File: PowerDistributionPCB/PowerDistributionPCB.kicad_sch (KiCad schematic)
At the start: 23 parts, among them J1 USB3_A, U1 Pico

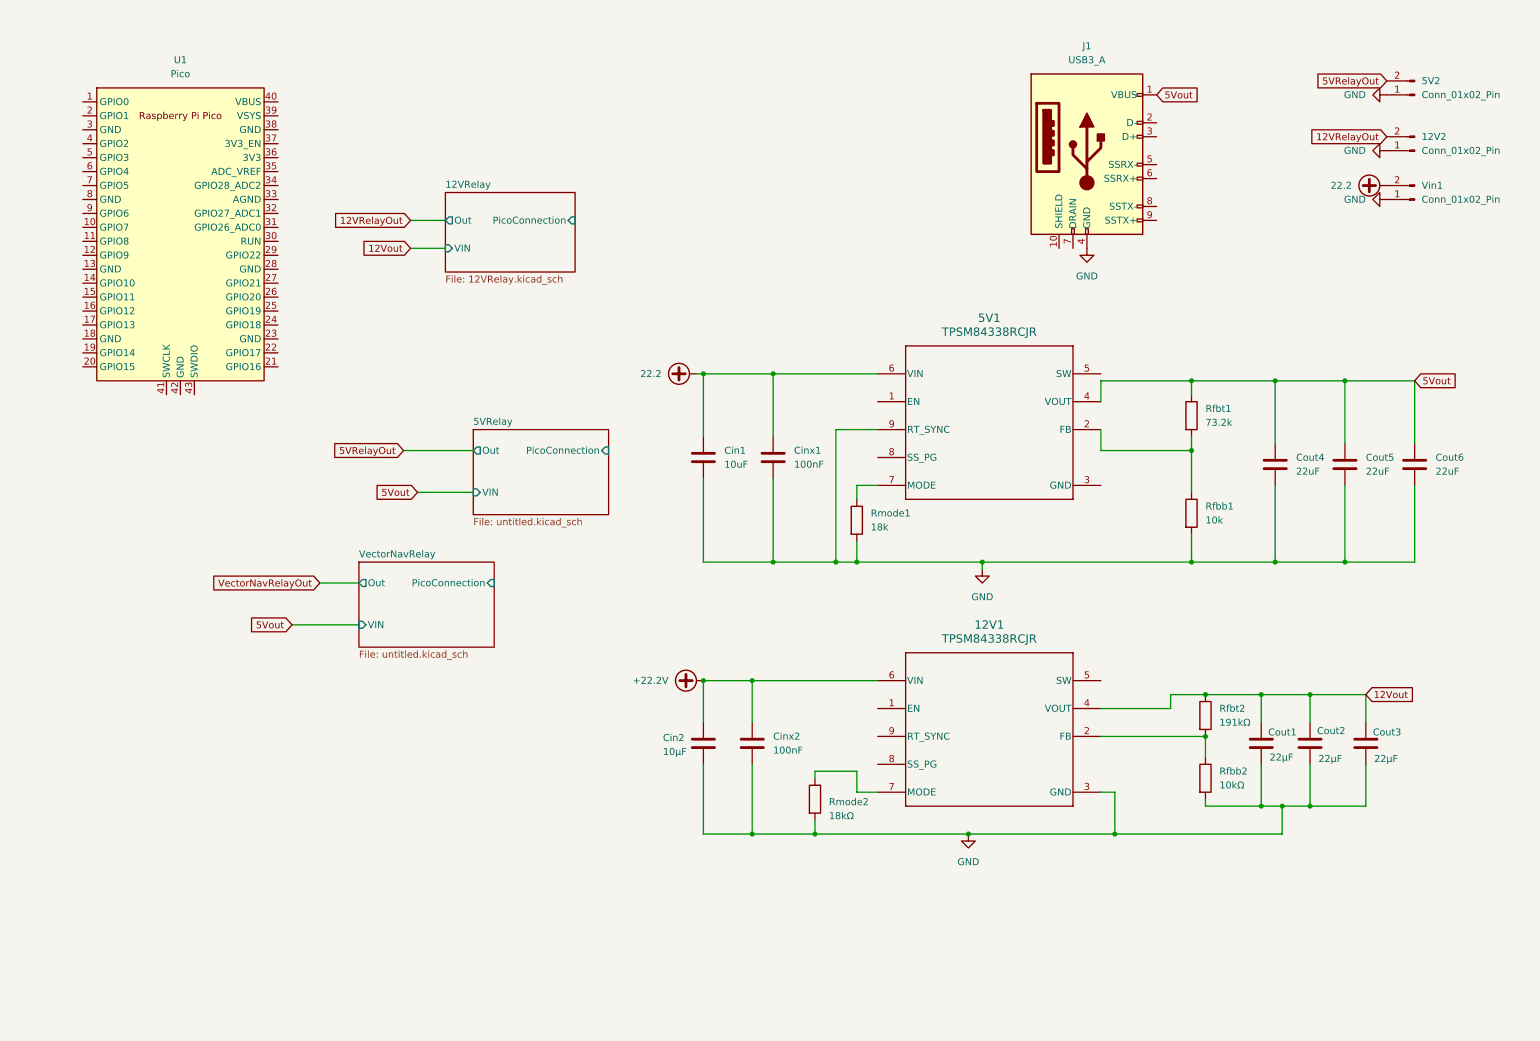
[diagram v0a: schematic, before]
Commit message: created sheet and updated USB connector
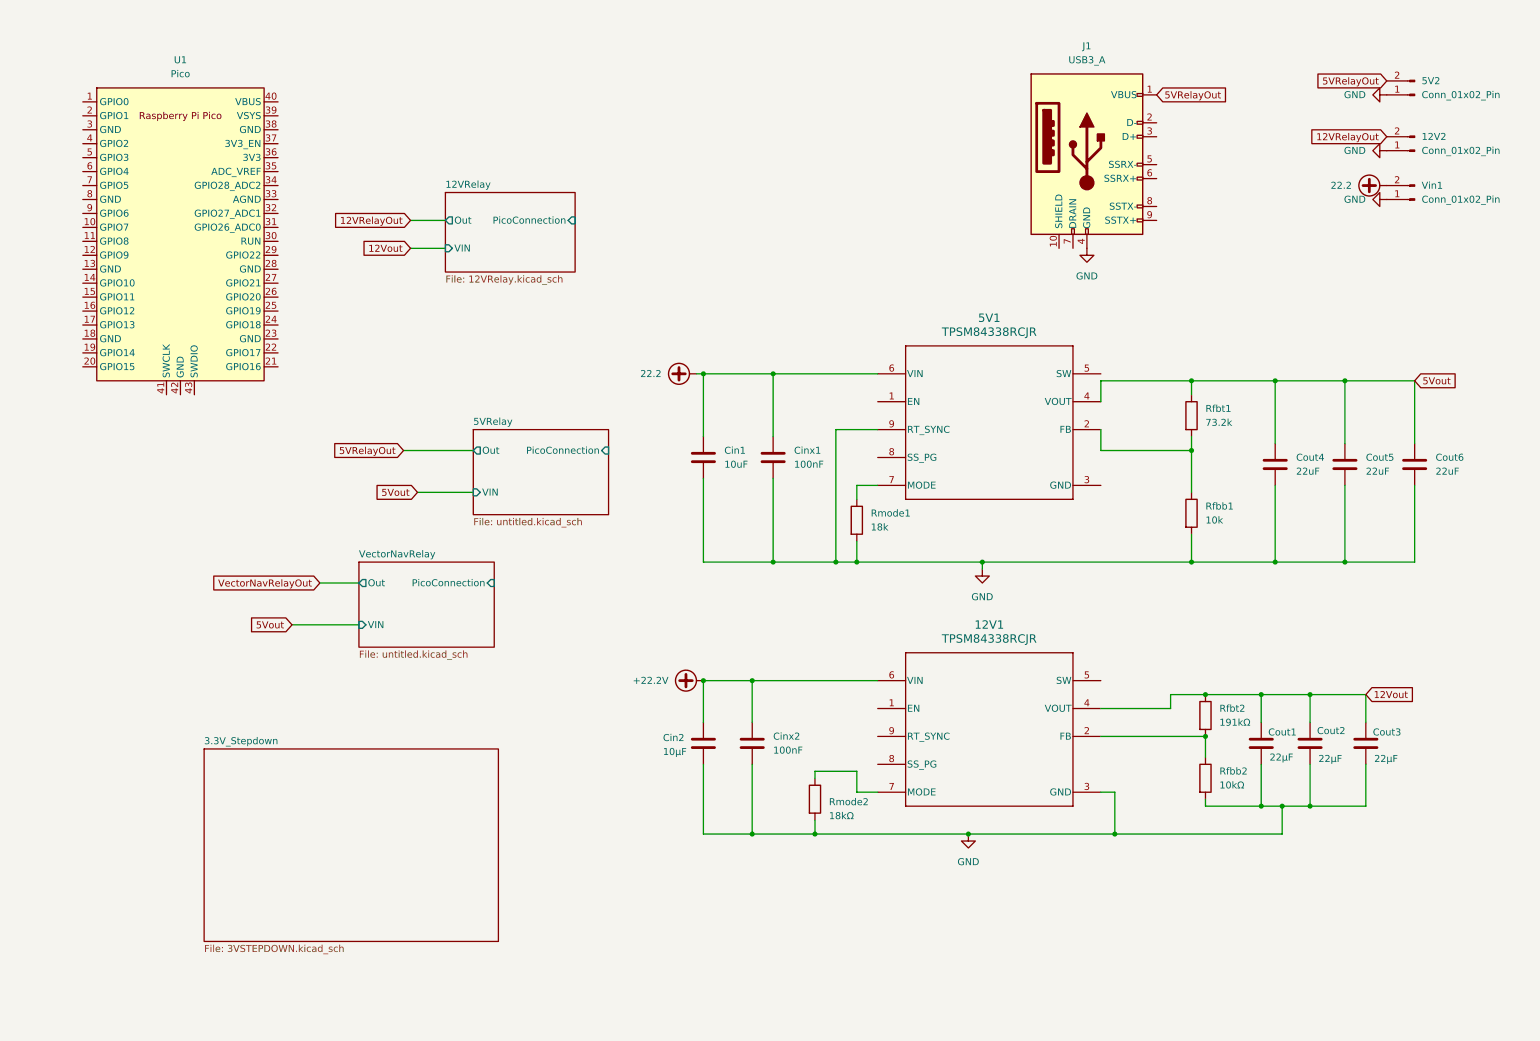
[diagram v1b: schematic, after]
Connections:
- net 5VRelayOut: now also J1.1 (VBUS)
- net 5Vout: no longer J1.1 (VBUS)
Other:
- added sheet 3.3V_Stepdown (3VSTEPDOWN.kicad_sch)
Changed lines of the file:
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@@
 		)
 	)
-	(global_label "5Vout"
+	(global_label "5VRelayOut"
 		(shape input)
-		(at 218.44 22.86 0)
+		(at 81.28 87.63 180)
 		(fields_autoplaced yes)
 		(effects
@@
 				(size 1.27 1.27)
 			)
-			(justify left)
+			(justify right)
 		)
 		(property "Intersheetrefs" "${INTERSHEET_REFS}"
-			(at 226.747 22.86 0)
-			(effects
-				(font
-					(size 1.27 1.27)
-				)
-				(justify left)
+			(at 67.6511 87.63 0)
+			(effects
+				(font
+					(size 1.27 1.27)
+				)
+				(justify right)
 				(hide yes)
 			)
@@
 	(global_label "5VRelayOut"
 		(shape input)
-		(at 81.28 87.63 180)
+		(at 218.44 22.86 0)
 		(fields_autoplaced yes)
 		(effects
@@
 				(size 1.27 1.27)
 			)
-			(justify right)
+			(justify left)
 		)
 		(property "Intersheetrefs" "${INTERSHEET_REFS}"
-			(at 67.6511 87.63 0)
-			(effects
-				(font
-					(size 1.27 1.27)
-				)
-				(justify right)
+			(at 232.0689 22.86 0)
+			(effects
+				(font
+					(size 1.27 1.27)
+				)
+				(justify left)
 				(hide yes)
 			)
@@
 				)
 			)
+		)
+	)
+	(sheet
+		(at 44.958 141.986)
+		(size 53.594 35.052)
+		(exclude_from_sim no)
+		(in_bom yes)
+		(on_board yes)
+		(dnp no)
+		(fields_autoplaced yes)
+		(stroke
+			(width 0.1524)
+			(type solid)
+		)
+		(fill
+			(color 0 0 0 0.0000)
+		)
+		(property "Sheetname" "3.3V_Stepdown"
+			(at 44.958 141.2744 0)
+			(effects
+				(font
+					(size 1.27 1.27)
+				)
+				(justify left bottom)
+			)
+		)
+		(property "Sheetfile" "3VSTEPDOWN.kicad_sch"
+			(at 44.958 177.6226 0)
+			(effects
+				(font
+					(size 1.27 1.27)
+				)
+				(justify left top)
+			)
+		)
+		(instances
+			(project "PowerDistributionPCB"
+				(path "/b27c75df-6223-4cc6-be69-062c2b02d5c6"
+					(page "5")
+				)
+			)

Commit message: switched pico to arduino, started implementing 3.3 relay and updated connections
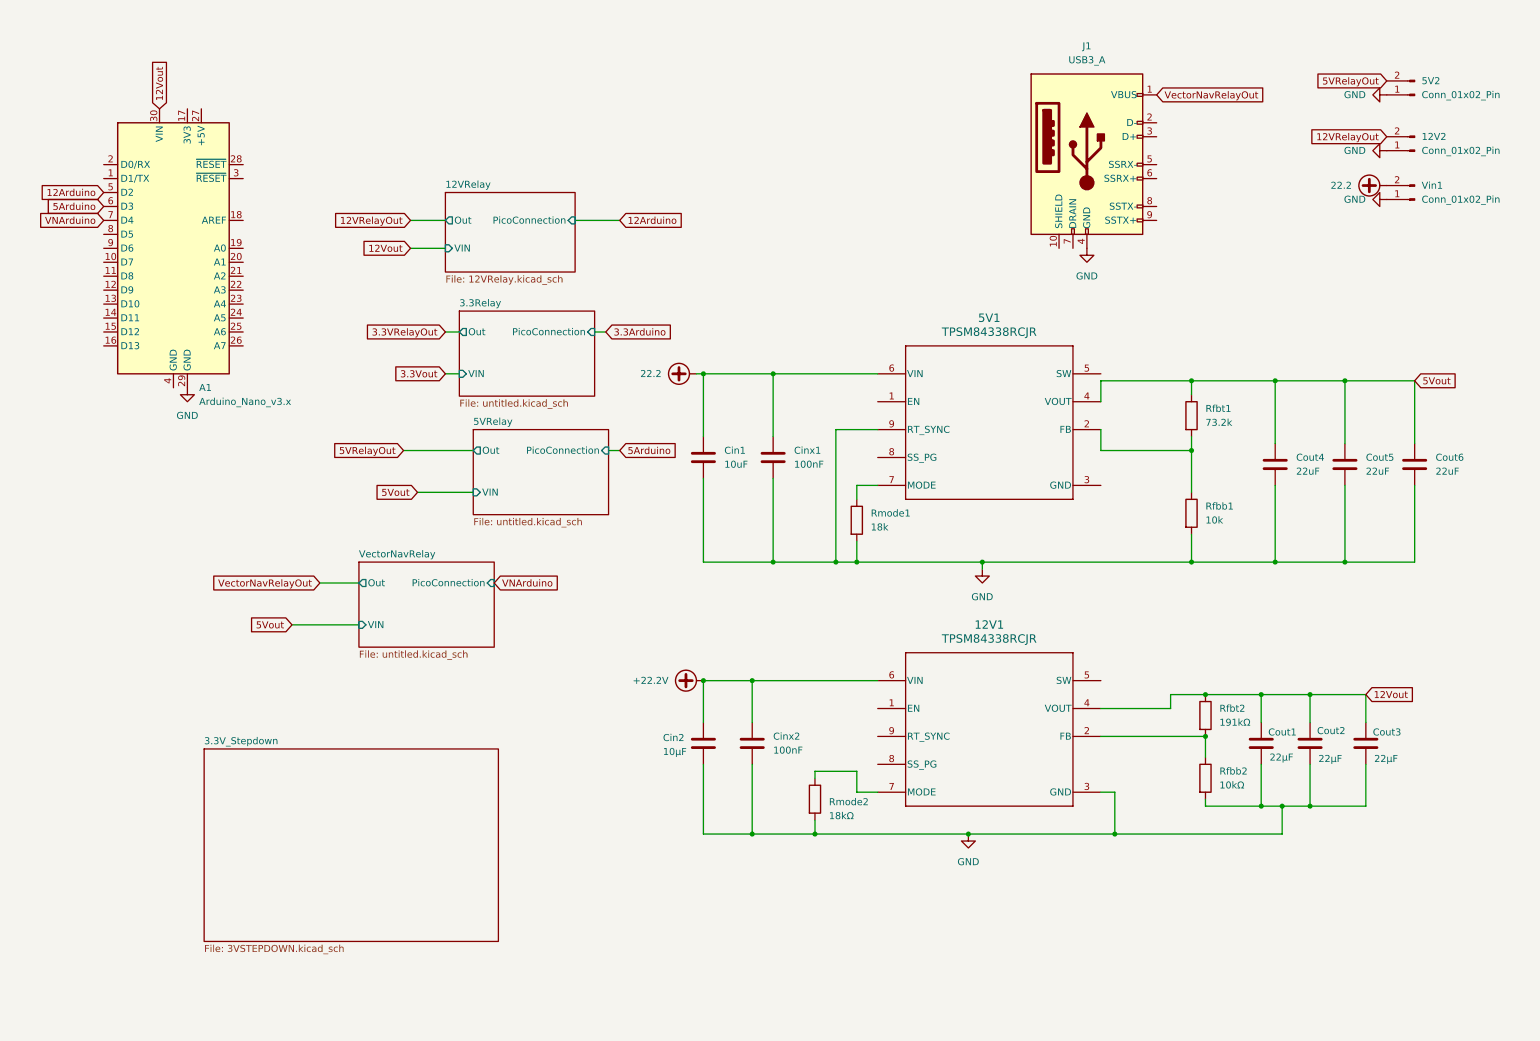
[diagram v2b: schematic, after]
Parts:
- removed U1: Pico, RPi_Pico:RPi_Pico_SMD_TH, symbol CustomComponents:Pico
- added A1: Arduino_Nano_v3.x, Module:Arduino_Nano, symbol MCU_Module:Arduino_Nano_v3.x
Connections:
- net 12Vout: now also A1.30 (VIN)
- net 5VRelayOut: no longer J1.1 (VBUS)
- net GND: now also A1.29 (GND)
- net VectorNavRelayOut: now also J1.1 (VBUS)
- new net 12Arduino: A1.5 (D2)
- new net 5Arduino: A1.6 (D3)
- new net VNArduino: A1.7 (D4)
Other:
- added sheet 3.3Relay (untitled.kicad_sch)

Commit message: started reworking relays for new relay design
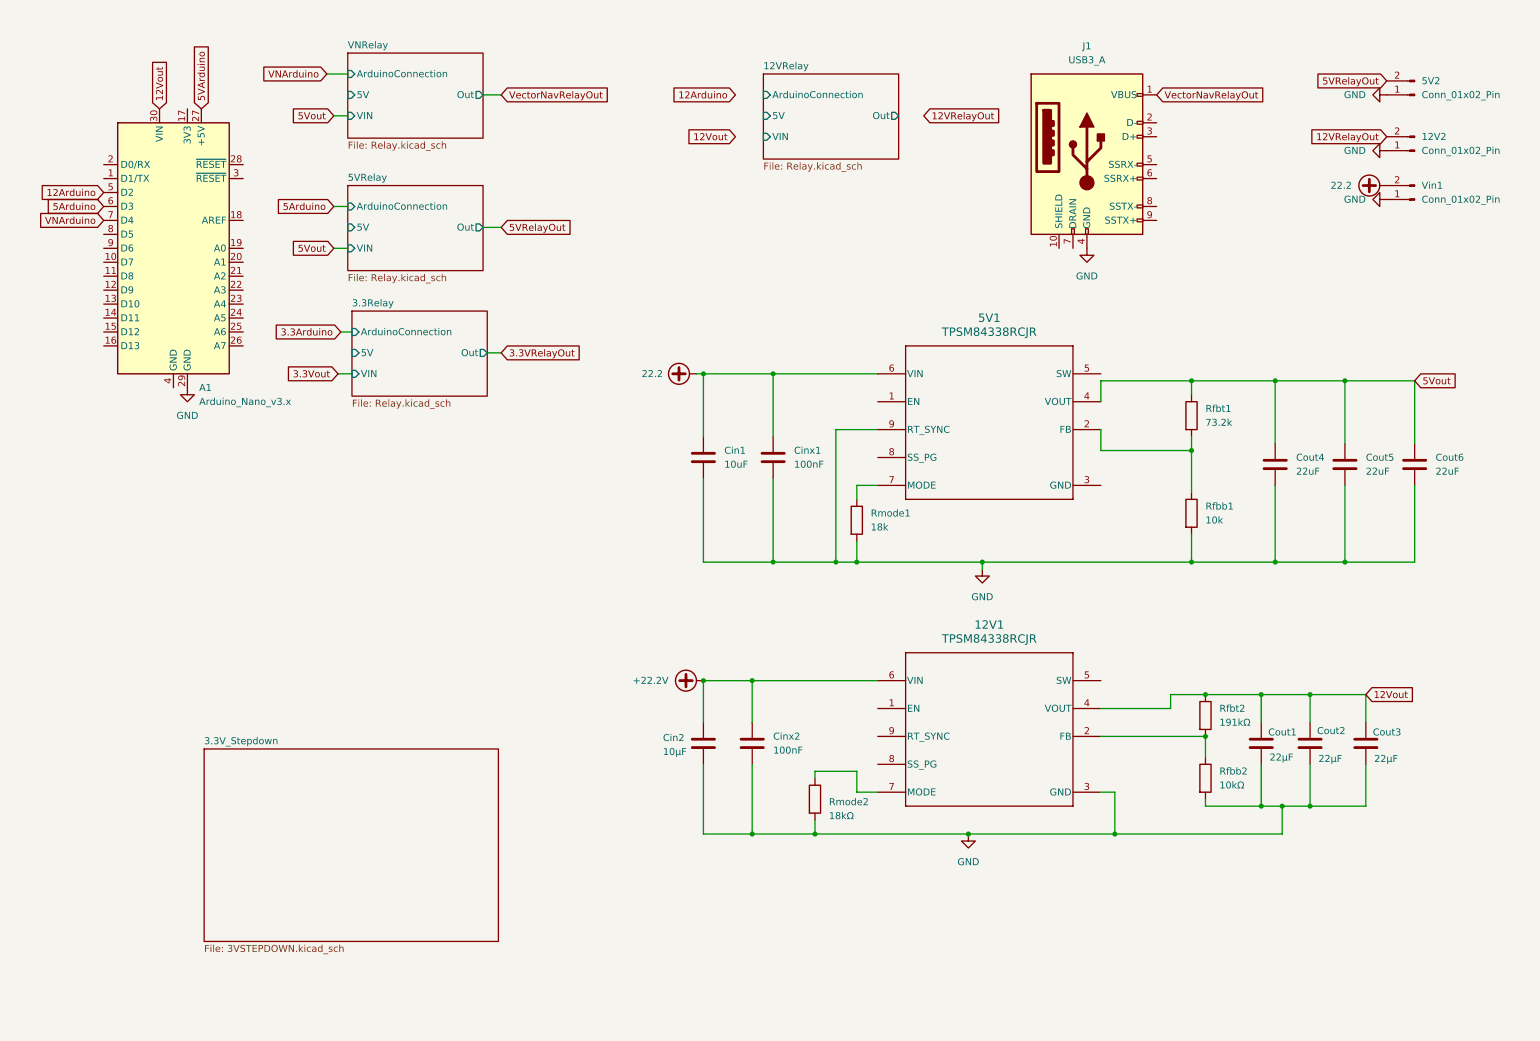
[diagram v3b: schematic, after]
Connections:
- net 5VArduino: now reaches A1.27 (+5V)
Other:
- removed sheet VectorNavRelay
- added sheet VNRelay (Relay.kicad_sch)
- sheet 12VRelay: file 12VRelay.kicad_sch -> Relay.kicad_sch
- sheet 12VRelay ports: added 5V, ArduinoConnection; removed PicoConnection
- sheet 3.3Relay: file untitled.kicad_sch -> Relay.kicad_sch
- sheet 3.3Relay ports: added 5V, ArduinoConnection; removed PicoConnection
- sheet 5VRelay: file untitled.kicad_sch -> Relay.kicad_sch
- sheet 5VRelay ports: added 5V, ArduinoConnection; removed PicoConnection

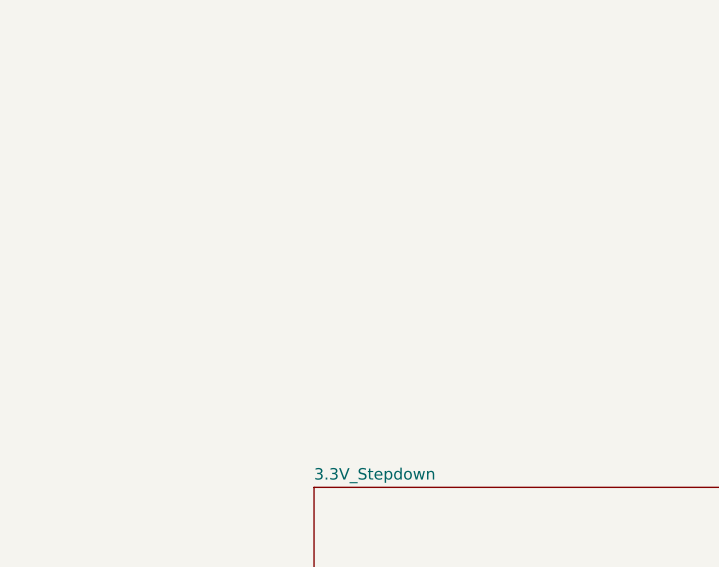
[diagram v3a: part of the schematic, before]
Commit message: added reverse polarity sheet
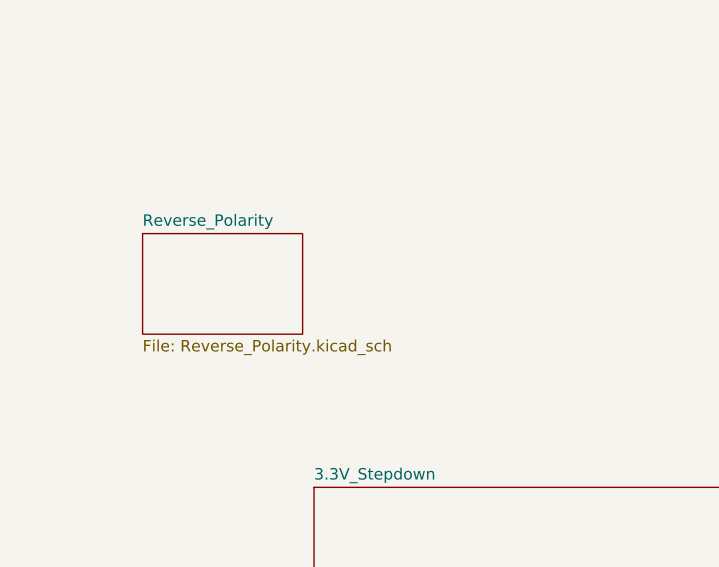
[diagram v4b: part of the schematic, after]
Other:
- added sheet Reverse_Polarity (Reverse_Polarity.kicad_sch)
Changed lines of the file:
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@@
+	)
+	(sheet
+		(at 25.908 113.792)
+		(size 17.78 11.176)
+		(exclude_from_sim no)
+		(in_bom yes)
+		(on_board yes)
+		(dnp no)
+		(fields_autoplaced yes)
+		(stroke
+			(width 0.1524)
+			(type solid)
+		)
+		(fill
+			(color 0 0 0 0.0000)
+		)
+		(property "Sheetname" "Reverse_Polarity"
+			(at 25.908 113.0804 0)
+			(effects
+				(font
+					(size 1.27 1.27)
+				)
+				(justify left bottom)
+			)
+		)
+		(property "Sheetfile" "Reverse_Polarity.kicad_sch"
+			(at 25.908 125.5526 0)
+			(effects
+				(font
+					(size 1.27 1.27)
+				)
+				(justify left top)
+			)
+		)
+		(instances
+			(project "PowerDistributionPCB"
+				(path "/b27c75df-6223-4cc6-be69-062c2b02d5c6"
+					(page "7")
+				)
+			)
+		)
 	)
 	(sheet
